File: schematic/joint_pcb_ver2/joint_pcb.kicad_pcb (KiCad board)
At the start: 2 copper layers, 100 x 100 mm, 43 parts, among them IC1 LM361N_NOPB, IC2 ADA4891-2ARMZ-R7, J1 Screw_Terminal_01x04, U1 LM324, U2 LM7805_TO220

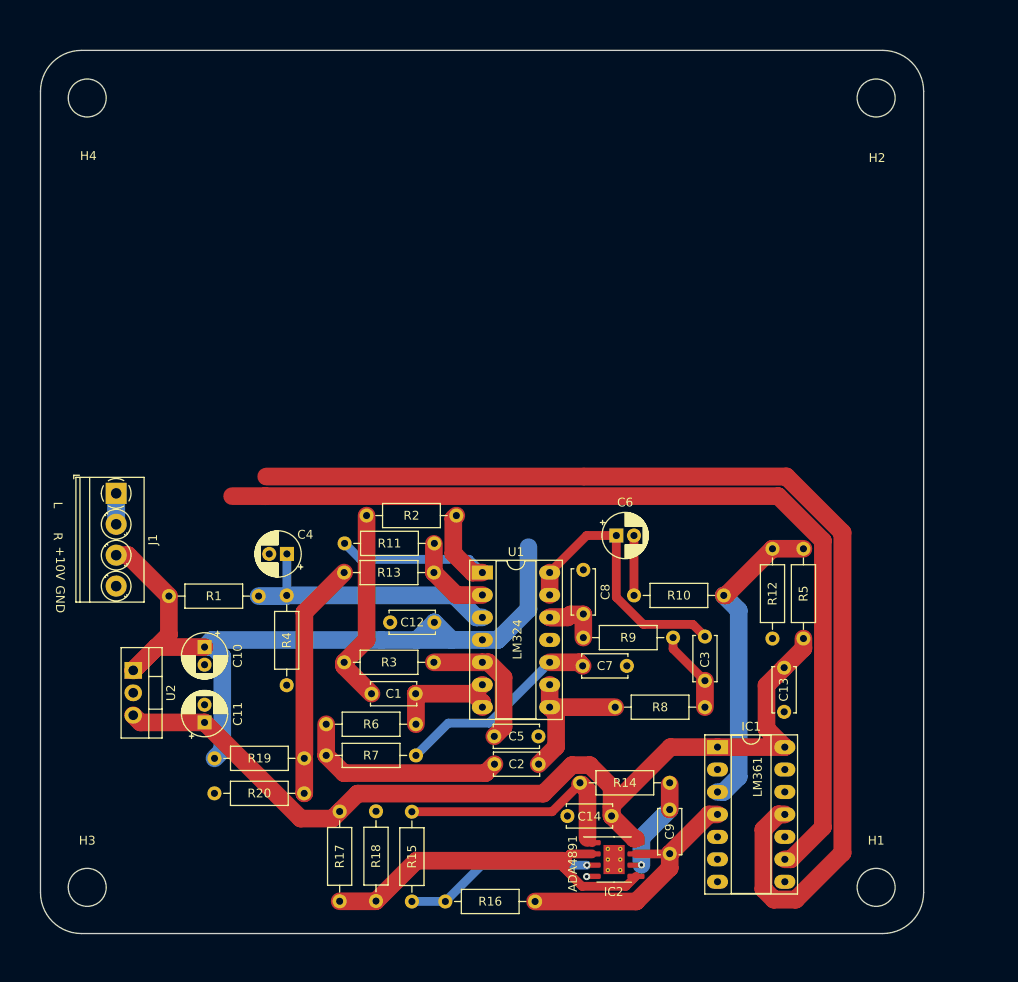
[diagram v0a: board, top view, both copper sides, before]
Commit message: connect up 10V
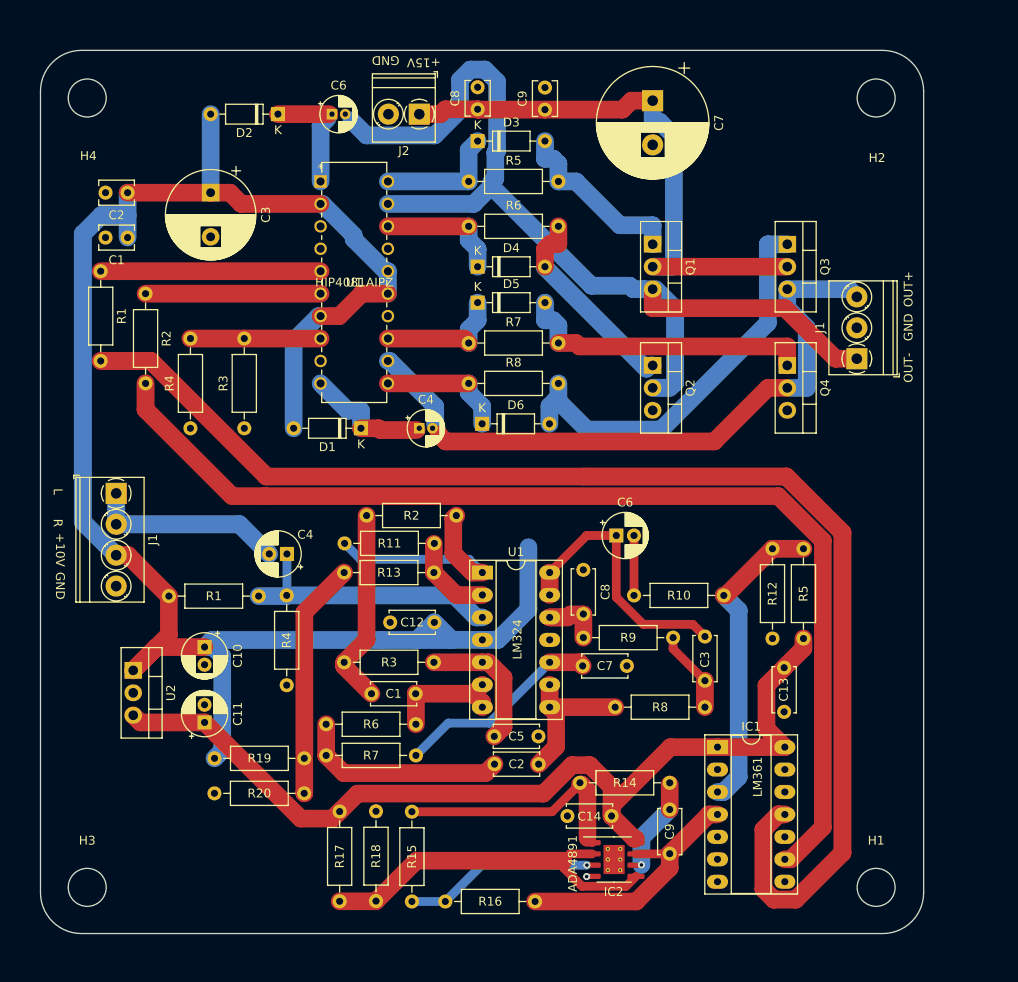
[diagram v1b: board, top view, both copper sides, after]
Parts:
- added C1: 10uF, Capacitor_THT:C_Disc_D3.8mm_W2.6mm_P2.50mm, F.Cu at (62.2, 66.0)
- added C2: 0.1uF, Capacitor_THT:C_Disc_D3.8mm_W2.6mm_P2.50mm, F.Cu at (62.2, 61.0)
- added C3: 100uF, Capacitor_THT:CP_Radial_D10.0mm_P5.00mm, F.Cu at (71.6, 61.0)
- added C4: 1uF, Capacitor_THT:CP_Radial_D4.0mm_P1.50mm, F.Cu at (95.2, 87.6)
- added C6: 1uF, Capacitor_THT:CP_Radial_D4.0mm_P1.50mm, F.Cu at (85.4, 52.1)
- added C7: 1000uF, Capacitor_THT:CP_Radial_D12.5mm_P5.00mm, F.Cu at (121.7, 50.5)
- added C8: 10uF, Capacitor_THT:C_Disc_D3.8mm_W2.6mm_P2.50mm, F.Cu at (101.9, 51.5)
- added C9: 0.1uF, Capacitor_THT:C_Disc_D3.8mm_W2.6mm_P2.50mm, F.Cu at (109.5, 51.6)
- added D1: 1N4148, Diode_THT:D_DO-35_SOD27_P7.62mm_Horizontal, F.Cu at (88.6, 87.6)
- added D2: 1N4148, Diode_THT:D_DO-35_SOD27_P7.62mm_Horizontal, F.Cu at (79.2, 52.1)
- added D3: 1N4148, Diode_THT:D_DO-35_SOD27_P7.62mm_Horizontal, F.Cu at (101.9, 55.1)
- added D4: 1N4148, Diode_THT:D_DO-35_SOD27_P7.62mm_Horizontal, F.Cu at (101.9, 69.3)
- added D5: 1N4148, Diode_THT:D_DO-35_SOD27_P7.62mm_Horizontal, F.Cu at (101.9, 73.4)
- added D6: 1N4148, Diode_THT:D_DO-35_SOD27_P7.62mm_Horizontal, F.Cu at (102.4, 87.1)
- added J1: Power_PWM_output, TerminalBlock_Phoenix:TerminalBlock_Phoenix_PT-1,5-3-3.5-H_1x03_P3.50mm_Horizontal, F.Cu at (144.8, 79.8)
- added J2: Amp_power, TerminalBlock_Phoenix:TerminalBlock_Phoenix_PT-1,5-2-3.5-H_1x02_P3.50mm_Horizontal, F.Cu at (95.2, 52.1)
- added Q1: IRF510PBF, Package_TO_SOT_THT:TO-220-3_Vertical, F.Cu at (121.7, 66.8)
- added Q2: IRF510PBF, Package_TO_SOT_THT:TO-220-3_Vertical, F.Cu at (121.7, 80.5)
- added Q3: IRF510PBF, Package_TO_SOT_THT:TO-220-3_Vertical, F.Cu at (136.9, 66.8)
- added Q4: IRF510PBF, Package_TO_SOT_THT:TO-220-3_Vertical, F.Cu at (136.9, 80.5)
- added R1: 470R, Resistor_THT:R_Axial_DIN0207_L6.3mm_D2.5mm_P10.16mm_Horizontal, F.Cu at (59.2, 69.8)
- added R2: 470R, Resistor_THT:R_Axial_DIN0207_L6.3mm_D2.5mm_P10.16mm_Horizontal, F.Cu at (64.3, 72.4)
- added R3: 47kR, Resistor_THT:R_Axial_DIN0207_L6.3mm_D2.5mm_P10.16mm_Horizontal, F.Cu at (75.4, 87.6)
- added R4: 47kR, Resistor_THT:R_Axial_DIN0207_L6.3mm_D2.5mm_P10.16mm_Horizontal, F.Cu at (69.3, 87.6)
- added R5: 100R, Resistor_THT:R_Axial_DIN0207_L6.3mm_D2.5mm_P10.16mm_Horizontal, F.Cu at (100.8, 59.7)
- added R6: 100R, Resistor_THT:R_Axial_DIN0207_L6.3mm_D2.5mm_P10.16mm_Horizontal, F.Cu at (100.8, 64.8)
- added R7: 100R, Resistor_THT:R_Axial_DIN0207_L6.3mm_D2.5mm_P10.16mm_Horizontal, F.Cu at (100.8, 78.0)
- added R8: 100R, Resistor_THT:R_Axial_DIN0207_L6.3mm_D2.5mm_P10.16mm_Horizontal, F.Cu at (100.8, 82.5)
- added U1: HIP4081AIPZ, footprints:HIP4081AIPZ, F.Cu at (84.1, 59.7)
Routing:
- net Vcc: track 93.8 -> 210.3 mm
- net BHS: track 0.00 -> 113.2 mm
- net AHS: track 0.00 -> 75.9 mm
- net +15V: track 0.00 -> 64.9 mm
- net Net-(D6-Pad2): track 0.00 -> 46.4 mm
- net Net-(D5-Pad2): track 0.00 -> 34.0 mm
- net Net-(R1-Pad1): track 0.00 -> 24.9 mm
- net PWM+: track 125.6 -> 149.8 mm
- net Net-(D4-Pad2): track 0.00 -> 22.9 mm
- net Net-(D3-Pad2): track 0.00 -> 20.6 mm
- net Net-(R2-Pad1): track 0.00 -> 19.8 mm
- net Input: track 3.50 -> 22.2 mm
- net PWM-: track 107.2 -> 124.0 mm
- net Net-(R3-Pad2): track 0.00 -> 14.7 mm
- net Net-(C4-Pad1): track 31.1 -> 45.7 mm
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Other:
- board text added: "+15V"
- board text added: "OUT+"
- board text added: "OUT-"

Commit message: add text and zoon
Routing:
- added copper zone on B.Cu, net GND
- added copper zone on F.Cu, net GND
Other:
- board text added: "Author: Conagh Fitzgerald-Mansell Kebra Tajbe Louis Li"
- board text added: "Victoria University of Wellington ECEN405 Power Electronic D-Class Amplifier Input signal: -1V to +1V Power: 80 W max"

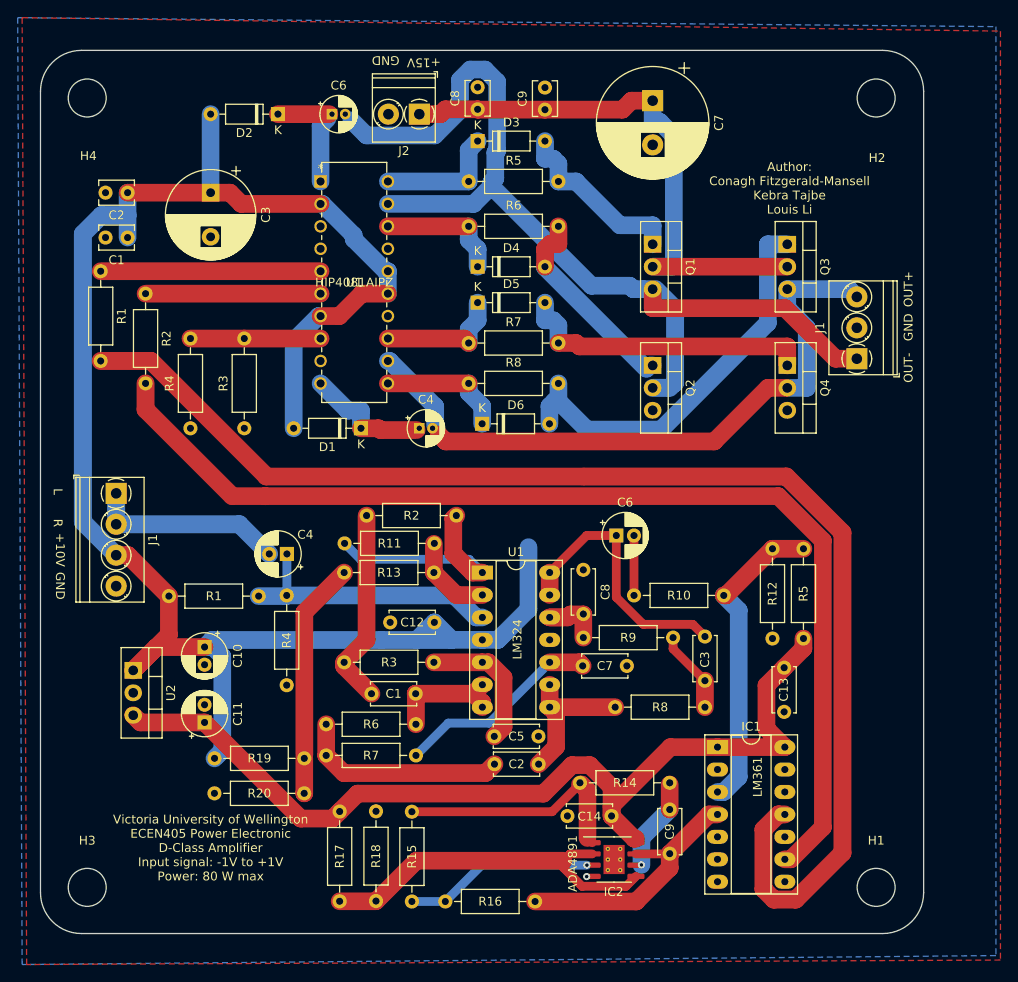
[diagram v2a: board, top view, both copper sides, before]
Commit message: Removed thermal vias from ADA4981
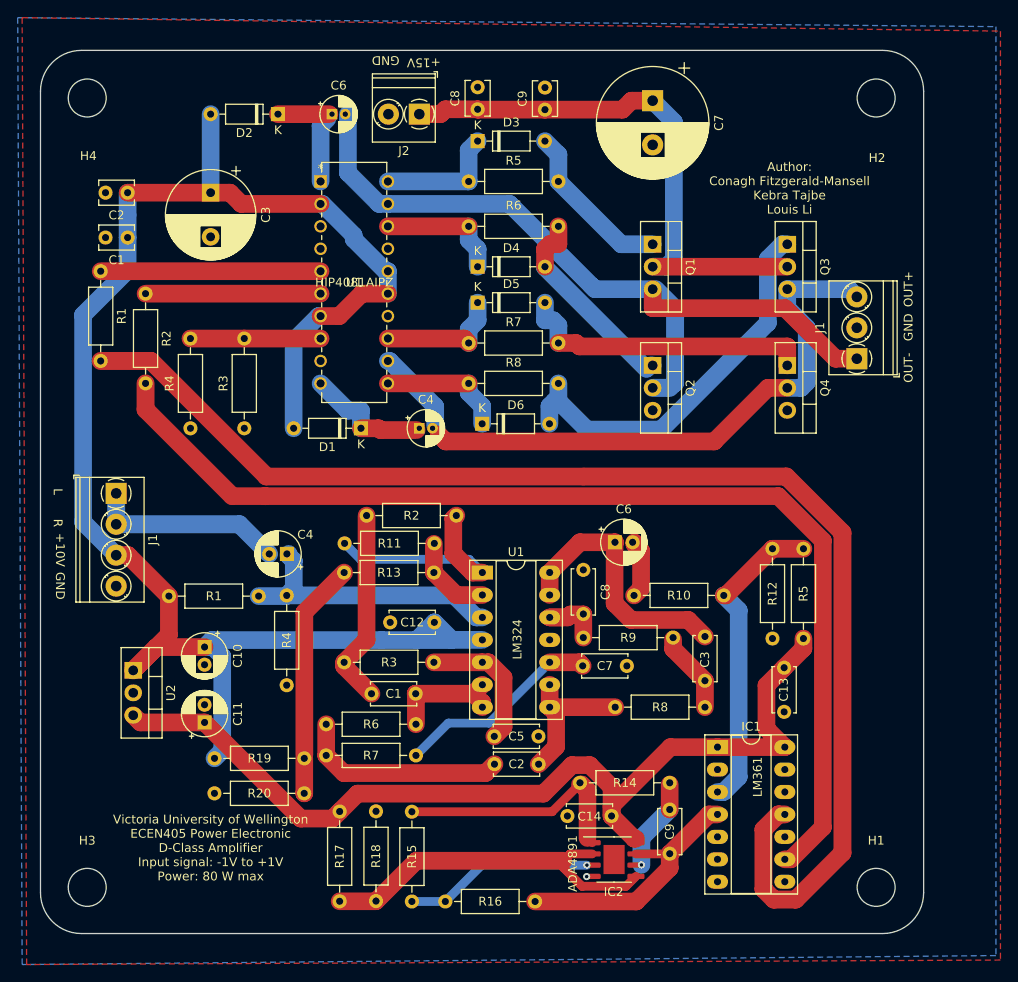
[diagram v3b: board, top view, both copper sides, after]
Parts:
- IC2: footprint Package_SO:SOIC-8-1EP_3.9x4.9mm_P1.27mm_EP2.41x3.3mm_ThermalVias -> Package_SO:SOIC-8-1EP_3.9x4.9mm_P1.27mm_EP2.41x3.3mm
- moved C6 0.78 mm to (117.4, 100.5)
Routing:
- net BHS: track 113.2 -> 88.2 mm
- net Vcc: track 210.3 -> 191.5 mm
- net Net-(D3-Pad2): track 20.6 -> 18.8 mm
- net Net-(D6-Pad2): track 46.4 -> 45.4 mm
- net +15V: track 64.9 -> 64.0 mm
- net Net-(C3-Pad1): track 30.7 -> 30.1 mm
- net Net-(C4-Pad1): track 45.7 -> 46.3 mm
